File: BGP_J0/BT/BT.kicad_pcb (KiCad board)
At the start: 2 copper layers, 28 x 25 mm, 20 parts, among them P1 CONN_01X02, P2 CONN_01X02, P3 CONN_01X04, P4 CONN_01X04, Q1 MMBF5457

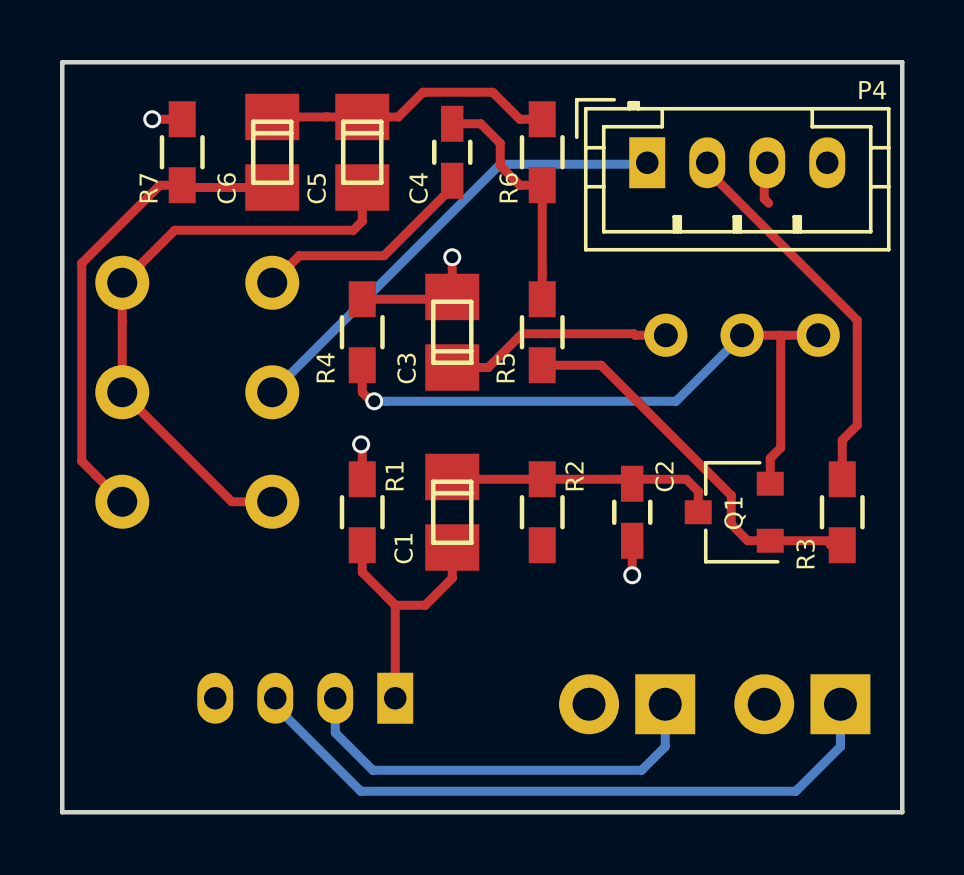
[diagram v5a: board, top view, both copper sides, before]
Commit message: Pots were out by a little, changed PCBs accordingly
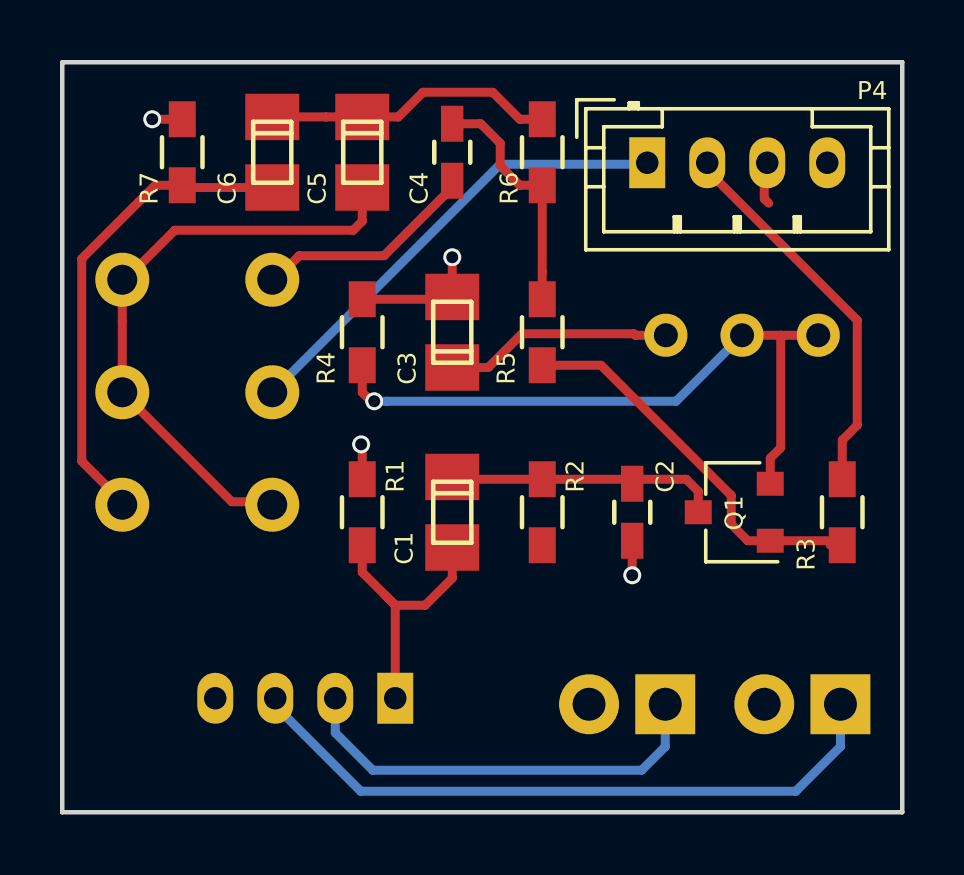
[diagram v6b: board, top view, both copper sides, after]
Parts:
- moved RV3 0.10 mm to (135.0, 93.8)
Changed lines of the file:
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@@
-    )
-  )
-  (module LIBS:Potentiometer_Alpha_Double_Vertical_Dual_Shaft (layer B.Cu)
-    (at 135 93.65 180)
-    (descr "Potentiometer, vertically mounted, Omeg PC16PU, Omeg PC16PU, Omeg PC16PU, Vishay/Spectrol 248GJ/249GJ Single, Vishay/Spectrol 248GJ/249GJ Single, Vishay/Spectrol 248GJ/249GJ Single, Vishay/Spectrol 248GH/249GH Single, Vishay/Spectrol 148/149 Single, Vishay/Spectrol 148/149 Single, Vishay/Spectrol 148/149 Single, Vishay/Spectrol 148A/149A Single with mounting plates, Vishay/Spectrol 148/149 Double, Vishay/Spectrol 148A/149A Double with mounting plates, Piher PC-16 Single, Piher PC-16 Single, Piher PC-16 Single, Piher PC-16SV Single, Piher PC-16 Double, Piher PC-16 Triple, Piher T16H Single, Piher T16L Single, Piher T16H Double, Alps RK163 Single, Alps RK163 Double, Alps RK097 Single, Alps RK097 Double, http://www.alps.com/prod/info/E/HTML/Potentiometer/RotaryPotentiometers/RK097/RK09712100AV.html")
-    (tags "Potentiometer vertical  Omeg PC16PU  Omeg PC16PU  Omeg PC16PU  Vishay/Spectrol 248GJ/249GJ Single  Vishay/Spectrol 248GJ/249GJ Single  Vishay/Spectrol 248GJ/249GJ Single  Vishay/Spectrol 248GH/249GH Single  Vishay/Spectrol 148/149 Single  Vishay/Spectrol 148/149 Single  Vishay/Spectrol 148/149 Single  Vishay/Spectrol 148A/149A Single with mounting plates  Vishay/Spectrol 148/149 Double  Vishay/Spectrol 148A/149A Double with mounting plates  Piher PC-16 Single  Piher PC-16 Single  Piher PC-16 Single  Piher PC-16SV Single  Piher PC-16 Double  Piher PC-16 Triple  Piher T16H Single  Piher T16L Single  Piher T16H Double  Alps RK163 Single  Alps RK163 Double  Alps RK097 Single  Alps RK097 Double Dual Shaft")
-    (fp_text reference RV3 (at -5.2 11.25 180) (layer B.SilkS)
-      (effects (font (size 0.6 0.6) (thickness 0.15)) (justify mirror))
-    )
-    (fp_text value DUAL_POT (at 2.15 -4 180) (layer B.Fab) hide
-      (effects (font (size 0.6 0.6) (thickness 0.15)) (justify mirror))
-    )
-    (fp_line (start -11.7 10.35) (end -11.7 -2.85) (layer B.Fab) (width 0.1))
-    (fp_line (start -11.7 -2.85) (end 1.8 -2.85) (layer B.Fab) (width 0.1))
-    (fp_line (start 1.8 -2.85) (end 1.8 10.35) (layer B.Fab) (width 0.1))
-    (fp_line (start 1.8 10.35) (end -11.7 10.35) (layer B.Fab) (width 0.1))
-    (fp_line (start -11.76 10.4) (end 1.86 10.4) (layer B.SilkS) (width 0.12))
-    (fp_line (start -11.76 -2.91) (end 1.86 -2.91) (layer B.SilkS) (width 0.12))
-    (fp_line (start -11.76 10.4) (end -11.76 -2.91) (layer B.SilkS) (width 0.12))
-    (fp_line (start 1.86 10.4) (end 1.86 -2.91) (layer B.SilkS) (width 0.12))
-    (fp_line (start -12.15 10.6) (end -12.15 -3.1) (layer B.CrtYd) (width 0.05))
-    (fp_line (start -12.15 -3.1) (end 2.1 -3.1) (layer B.CrtYd) (width 0.05))
-    (fp_line (start 2.1 -3.1) (end 2.1 10.6) (layer B.CrtYd) (width 0.05))
-    (fp_line (start 2.1 10.6) (end -12.15 10.6) (layer B.CrtYd) (width 0.05))
-    (pad 3 thru_hole circle (at 0 7.3 180) (size 1.8 1.8) (drill 1) (layers *.Cu *.Mask)
-      (net 8 /RV_4))
-    (pad 2 thru_hole circle (at 0 3.65 180) (size 1.8 1.8) (drill 1) (layers *.Cu *.Mask)
-      (net 8 /RV_4))
-    (pad 1 thru_hole circle (at 0 0 180) (size 1.8 1.8) (drill 1) (layers *.Cu *.Mask)
-      (net 9 /RV_1))
-    (pad 6 thru_hole circle (at -5 7.3 180) (size 1.8 1.8) (drill 1) (layers *.Cu *.Mask)
-      (net 6 /RV_6))
-    (pad 5 thru_hole circle (at -5 3.65 180) (size 1.8 1.8) (drill 1) (layers *.Cu *.Mask)
-      (net 12 /OUT))
-    (pad 4 thru_hole circle (at -5 0 180) (size 1.8 1.8) (drill 1) (layers *.Cu *.Mask)
-      (net 8 /RV_4))
-    (model Potentiometers.3dshapes/Potentiometer_Alps_RK097_Double_Vertical.wrl
-      (at (xyz 0 0 0))
-      (scale (xyz 0.393701 0.393701 0.393701))
-      (rotate (xyz 0 0 0))
     )
   )
@@
       (at (xyz 0 0 0))
       (scale (xyz 1 1 1))
+      (rotate (xyz 0 0 0))
+    )
+  )
+  (module LIBS:Potentiometer_Alpha_Double_Vertical_Dual_Shaft (layer B.Cu)
+    (at 135 93.75 180)
+    (descr "Potentiometer, vertically mounted, Omeg PC16PU, Omeg PC16PU, Omeg PC16PU, Vishay/Spectrol 248GJ/249GJ Single, Vishay/Spectrol 248GJ/249GJ Single, Vishay/Spectrol 248GJ/249GJ Single, Vishay/Spectrol 248GH/249GH Single, Vishay/Spectrol 148/149 Single, Vishay/Spectrol 148/149 Single, Vishay/Spectrol 148/149 Single, Vishay/Spectrol 148A/149A Single with mounting plates, Vishay/Spectrol 148/149 Double, Vishay/Spectrol 148A/149A Double with mounting plates, Piher PC-16 Single, Piher PC-16 Single, Piher PC-16 Single, Piher PC-16SV Single, Piher PC-16 Double, Piher PC-16 Triple, Piher T16H Single, Piher T16L Single, Piher T16H Double, Alps RK163 Single, Alps RK163 Double, Alps RK097 Single, Alps RK097 Double, http://www.alps.com/prod/info/E/HTML/Potentiometer/RotaryPotentiometers/RK097/RK09712100AV.html")
+    (tags "Potentiometer vertical  Omeg PC16PU  Omeg PC16PU  Omeg PC16PU  Vishay/Spectrol 248GJ/249GJ Single  Vishay/Spectrol 248GJ/249GJ Single  Vishay/Spectrol 248GJ/249GJ Single  Vishay/Spectrol 248GH/249GH Single  Vishay/Spectrol 148/149 Single  Vishay/Spectrol 148/149 Single  Vishay/Spectrol 148/149 Single  Vishay/Spectrol 148A/149A Single with mounting plates  Vishay/Spectrol 148/149 Double  Vishay/Spectrol 148A/149A Double with mounting plates  Piher PC-16 Single  Piher PC-16 Single  Piher PC-16 Single  Piher PC-16SV Single  Piher PC-16 Double  Piher PC-16 Triple  Piher T16H Single  Piher T16L Single  Piher T16H Double  Alps RK163 Single  Alps RK163 Double  Alps RK097 Single  Alps RK097 Double Dual Shaft")
+    (fp_text reference RV3 (at -5.2 11.35 180) (layer B.SilkS)
+      (effects (font (size 0.6 0.6) (thickness 0.15)) (justify mirror))
+    )
+    (fp_text value DUAL_POT (at 2.15 -3.9 180) (layer B.Fab) hide
+      (effects (font (size 0.6 0.6) (thickness 0.15)) (justify mirror))
+    )
+    (fp_line (start -11.7 10.45) (end -11.7 -2.75) (layer B.Fab) (width 0.1))
+    (fp_line (start -11.7 -2.75) (end 1.8 -2.75) (layer B.Fab) (width 0.1))
+    (fp_line (start 1.8 -2.75) (end 1.8 10.45) (layer B.Fab) (width 0.1))
+    (fp_line (start 1.8 10.45) (end -11.7 10.45) (layer B.Fab) (width 0.1))
+    (fp_line (start -11.76 10.5) (end 1.86 10.5) (layer B.SilkS) (width 0.12))
+    (fp_line (start -11.76 -2.81) (end 1.86 -2.81) (layer B.SilkS) (width 0.12))
+    (fp_line (start -11.76 10.5) (end -11.76 -2.81) (layer B.SilkS) (width 0.12))
+    (fp_line (start 1.86 10.5) (end 1.86 -2.81) (layer B.SilkS) (width 0.12))
+    (fp_line (start -12.15 10.7) (end -12.15 -3) (layer B.CrtYd) (width 0.05))
+    (fp_line (start -12.15 -3) (end 2.1 -3) (layer B.CrtYd) (width 0.05))
+    (fp_line (start 2.1 -3) (end 2.1 10.7) (layer B.CrtYd) (width 0.05))
+    (fp_line (start 2.1 10.7) (end -12.15 10.7) (layer B.CrtYd) (width 0.05))
+    (pad 3 thru_hole circle (at 0 7.5 180) (size 1.8 1.8) (drill 1) (layers *.Cu *.Mask)
+      (net 8 /RV_4))
+    (pad 2 thru_hole circle (at 0 3.75 180) (size 1.8 1.8) (drill 1) (layers *.Cu *.Mask)
+      (net 8 /RV_4))
+    (pad 1 thru_hole circle (at 0 0 180) (size 1.8 1.8) (drill 1) (layers *.Cu *.Mask)
+      (net 9 /RV_1))
+    (pad 6 thru_hole circle (at -5 7.5 180) (size 1.8 1.8) (drill 1) (layers *.Cu *.Mask)
+      (net 6 /RV_6))
+    (pad 5 thru_hole circle (at -5 3.75 180) (size 1.8 1.8) (drill 1) (layers *.Cu *.Mask)
+      (net 12 /OUT))
+    (pad 4 thru_hole circle (at -5 0 180) (size 1.8 1.8) (drill 1) (layers *.Cu *.Mask)
+      (net 8 /RV_4))
+    (model Potentiometers.3dshapes/Potentiometer_Alps_RK097_Double_Vertical.wrl
+      (at (xyz 0 0 0))
+      (scale (xyz 0.393701 0.393701 0.393701))
       (rotate (xyz 0 0 0))
     )
@@
   (segment (start 135 90) (end 138.65 93.65) (width 0.3) (layer F.Cu) (net 8))
   (segment (start 138.65 93.65) (end 140 93.65) (width 0.3) (layer F.Cu) (net 8))
-  (segment (start 137 83.1) (end 136.25 83.1) (width 0.3) (layer F.Cu) (net 9))
-  (segment (start 133.649999 85.700001) (end 133.649999 92.299999) (width 0.3) (layer F.Cu) (net 9))
-  (segment (start 136.25 83.1) (end 133.649999 85.700001) (width 0.3) (layer F.Cu) (net 9))
+  (segment (start 137 83.1) (end 136.1 83.1) (width 0.3) (layer F.Cu) (net 9))
+  (segment (start 136.1 83.1) (end 133.649999 85.550001) (width 0.3) (layer F.Cu) (net 9))
   (segment (start 133.649999 92.299999) (end 134.100001 92.750001) (width 0.3) (layer F.Cu) (net 9))
+  (segment (start 133.649999 85.550001) (end 133.649999 92.299999) (width 0.3) (layer F.Cu) (net 9))
   (segment (start 134.100001 92.750001) (end 135 93.65) (width 0.3) (layer F.Cu) (net 9))
   (segment (start 140 83.17602) (end 137.07602 83.17602) (width 0.3) (layer F.Cu) (net 9))

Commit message: Changed Gain structure a bit
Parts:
- R1: value 499k -> 1.5MEG
- R3: value 12k -> 10k
- R4: value 6.8k -> 4.99k
- R7: value 1.5k -> 2k
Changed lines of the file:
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@@
-(kicad_pcb (version 4) (host pcbnew 4.0.4-1.fc24-product)
+(kicad_pcb (version 4) (host pcbnew 4.0.7)
   (general
     (links 34)
@@
       (effects (font (size 0.6 0.6) (thickness 0.15)))
     )
-    (fp_text value 499k (at 0 1.9 90) (layer F.Fab) hide
+    (fp_text value 1.5MEG (at 0 1.9 90) (layer F.Fab) hide
       (effects (font (size 0.6 0.6) (thickness 0.15)))
     )
@@
       (effects (font (size 0.6 0.6) (thickness 0.15)))
     )
-    (fp_text value 12k (at 0 1.9 270) (layer F.Fab) hide
+    (fp_text value 10k (at 0 1.9 270) (layer F.Fab) hide
       (effects (font (size 0.6 0.6) (thickness 0.15)))
     )
@@
       (effects (font (size 0.6 0.6) (thickness 0.15)))
     )
-    (fp_text value 6.8k (at 0 1.9 90) (layer F.Fab) hide
+    (fp_text value 4.99k (at 0 1.9 90) (layer F.Fab) hide
       (effects (font (size 0.6 0.6) (thickness 0.15)))
     )
@@
       (effects (font (size 0.6 0.6) (thickness 0.15)))
     )
-    (fp_text value 1.5k (at 0 1.9 90) (layer F.Fab) hide
-      (effects (font (size 0.6 0.6) (thickness 0.15)))
-    )
+    (fp_text value 2k (at 0 1.9 90) (layer F.Fab) hide
+      (effects (font (size 0.6 0.6) (thickness 0.15)))
+    )

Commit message: Value and gain structure tweak
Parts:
- R7: value 2k -> 1.8k
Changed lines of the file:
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@@
       (effects (font (size 0.6 0.6) (thickness 0.15)))
     )
-    (fp_text value 2k (at 0 1.9 90) (layer F.Fab) hide
+    (fp_text value 1.8k (at 0 1.9 90) (layer F.Fab) hide
       (effects (font (size 0.6 0.6) (thickness 0.15)))
     )
